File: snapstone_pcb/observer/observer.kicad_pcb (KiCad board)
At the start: 2 copper layers, 80 x 80 mm, 3 parts, among them Q1 NJFET, U1 ZRE200GE_Motion_Sensor

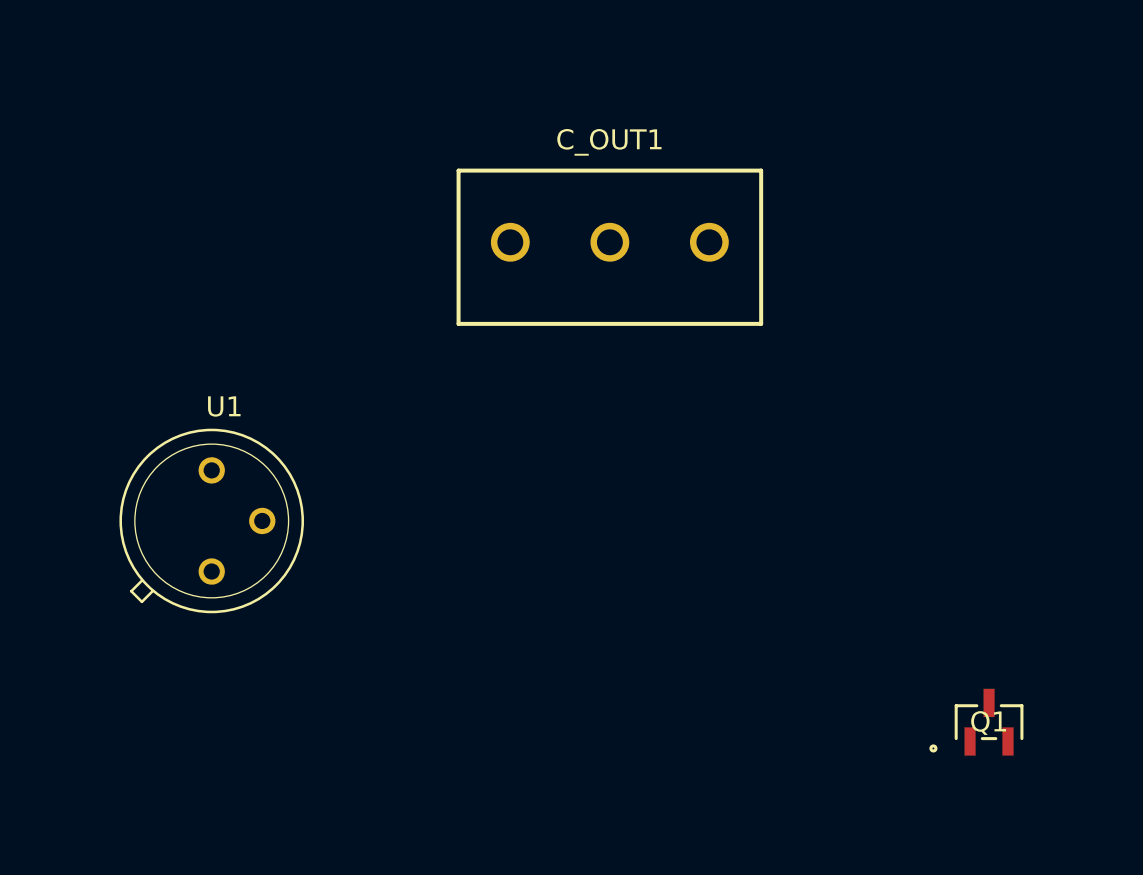
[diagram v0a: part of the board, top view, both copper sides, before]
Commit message: Updated resistor footprint project-wide
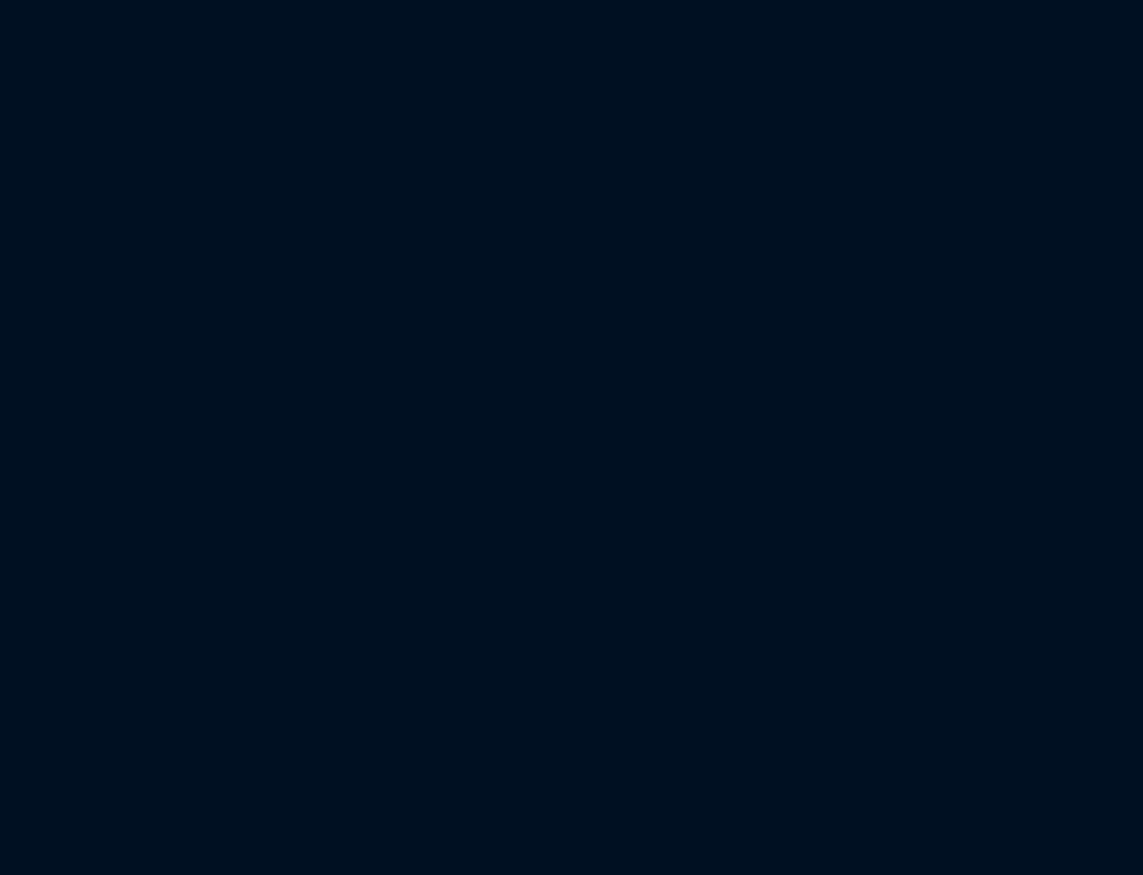
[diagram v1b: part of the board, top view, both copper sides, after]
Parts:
- removed C_OUT1: ~, 691137710003_Board_To_Wire:691137710003_Board_To_Wire
- removed Q1: NJFET, MMBFJ112_Analog_Switch:SOT-23_ONS
- removed U1: ZRE200GE_Motion_Sensor, ZRE200GE_Motion_Sensor:TO5

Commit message: Made PCB for observer & redstone block!
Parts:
- added BT1: 2468_Battery_Holder, 2468_Battery_Holder:BAT_2468, F.Cu at (150.0, 63.0)
- added C_OFF_IN1: ~, 691137710003_Board_To_Wire:691137710003_Board_To_Wire, F.Cu at (116.0, 90.0)
- added C_OUT1: ~, 691137710003_Board_To_Wire:691137710003_Board_To_Wire, F.Cu at (184.0, 90.0)
- added Q1: MMBFJ270_Analog_Switch, MMBFJ270_Analog_Switch:SOT-23_ONS, F.Cu at (149.0, 80.0)
- added R1: 150 Ω, CF12JT_Resistor:STA_CF12_STP, F.Cu at (173.9, 85.0)
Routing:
- net GND: track 0.00 -> 109.2 mm
- net VCC: track 0.00 -> 95.9 mm, vias 0 -> 1
- net Net-(C_OFF_IN1-DAT): track 0.00 -> 37.8 mm
- net Net-(Q1-D): track 0.00 -> 12.6 mm
- net Net-(C_OUT1-DAT): track 0.00 -> 10.1 mm
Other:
- board size 80 x 80 mm -> 80 x 50 mm
- board text added: "Border of 3D Part"
- board text added: "Observer Back"
- board text added: "Observer Front"

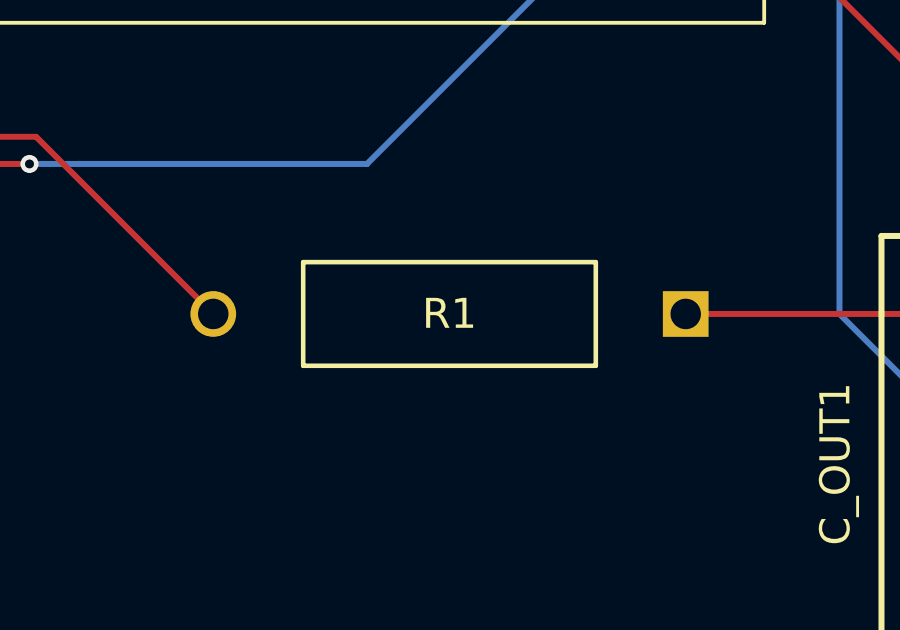
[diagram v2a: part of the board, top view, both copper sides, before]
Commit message: Fixed a problem in observer PCB
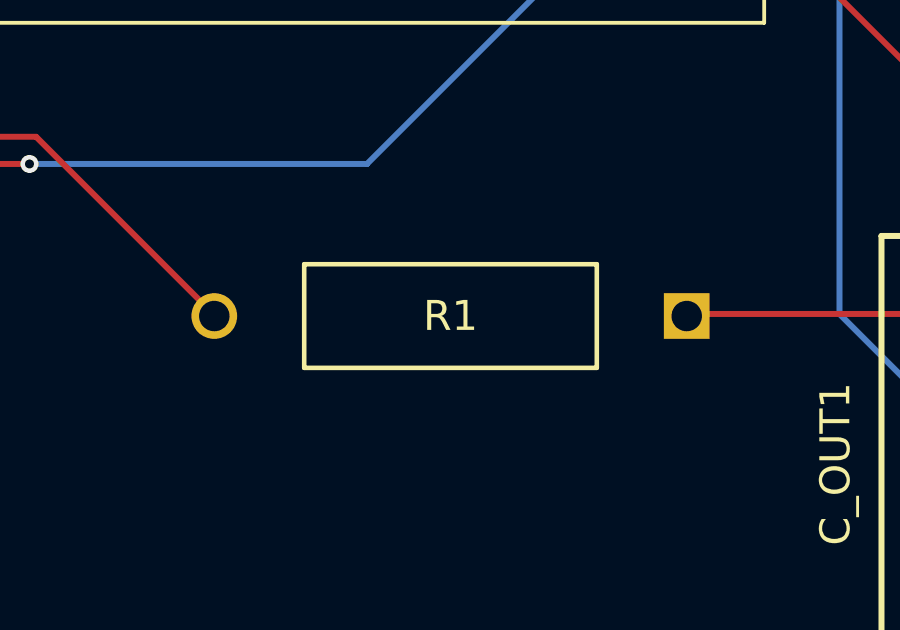
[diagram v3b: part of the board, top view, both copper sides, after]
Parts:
- moved R1 0.08 mm to (173.9, 85.1)
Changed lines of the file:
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@@
 	(footprint "CF12JT_Resistor:STA_CF12_STP"
 		(layer "F.Cu")
-		(at 173.874 85 180)
+		(at 173.9078 85.0696 180)
 		(tags "CF12JT150R ")
 		(property "Reference" "R1"
@@
 		)
 		(property "Value" "150 Ω"
-			(at 7.874 -3 0)
+			(at 7.9078 -2.9304 0)
 			(unlocked yes)
 			(layer "F.Fab")
@@
 		)
 		(embedded_fonts no)
-		(model "${SNAPSTONE_PARTS}/CF12JT150R_Resistor_150/CF12JT150R_Resistor_150.step"
+		(model "${SNAPSTONE_PARTS}/CF12JT_Resistor/CF12JT_Resistor.step"
 			(offset
 				(xyz 0 0 0)
